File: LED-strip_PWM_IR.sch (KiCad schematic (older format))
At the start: 18 parts, among them IC1 ATTINY85-S, P1 CONN_2, P2 CONN_2, Q1 8MHz, T1 IRLR2905_DPAK, U1 TSOP38238, U2 MCP1804-SOT23-5

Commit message: Grmbl! Never trust footprints from 'some lib'...
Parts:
- IC1: footprint SO8-200 -> (none)
- Q1: footprint murata-resonators-CSTLA_T -> (none)
- R3: value 20k -> 100k
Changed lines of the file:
@@
 F 0 "Q1" H 4400 2550 50  0000 L BNN
 F 1 "8MHz" H 4550 2550 50  0000 L BNN
-F 2 "murata-resonators-CSTLA_T" H 4550 2550 50  0001 C CNN
+F 2 "" H 4550 2550 50  0001 C CNN
 F 3 "" H 4550 2400 60  0001 C CNN
 	1    4550 2400
@@
 P 4100 3750
 F 0 "R3" V 4100 3850 50  0000 C CNN
-F 1 "20k" V 4100 3700 43  0000 C CNN
+F 1 "100k" V 4100 3700 43  0000 C CNN
 F 2 "" H 4100 3750 60  0001 C CNN
 F 3 "" H 4100 3750 60  0001 C CNN
@@
 F 0 "IC1" H 1900 1800 60  0000 C CNN
 F 1 "ATTINY85-S" H 3800 1000 60  0000 C CNN
-F 2 "SO8-200" H 2050 1000 60  0000 C CNN
+F 2 "" H 2050 1000 60  0000 C CNN
 F 3 "" H 2950 1400 60  0001 C CNN
 	1    2950 1400

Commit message: Switched Schottky diode to SS14L + rounded corners.
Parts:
- DS1: value MBRS140T3G -> SS14L
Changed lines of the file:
@@
 Sheet 1 1
 Title "LED-strip_PWM_IR"
-Date "19 may 2013"
-Rev "0.4"
+Date "16 Jun 2013"
+Rev "0.43"
 Comp "2013 - blog.spitzenpfeil.org"
 Comment1 ""
@@
 P 5500 3250
 F 0 "DS1" H 5500 3350 40  0000 C CNN
-F 1 "MBRS140T3G" H 5500 3150 40  0000 C CNN
+F 1 "SS14L" H 5500 3150 40  0000 C CNN
 F 2 "~" H 5500 3250 60  0000 C CNN
 F 3 "~" H 5500 3250 60  0000 C CNN

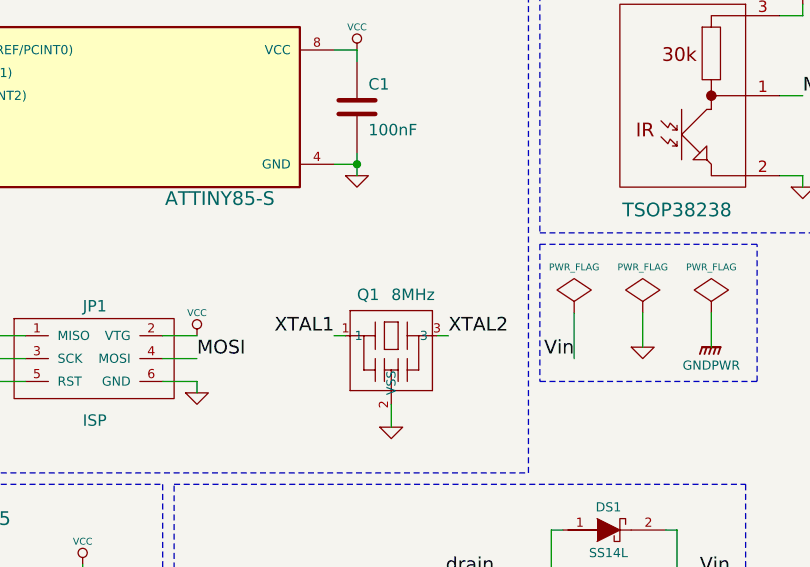
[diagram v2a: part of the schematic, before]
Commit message: Fixed resonator footprint (library part was off).
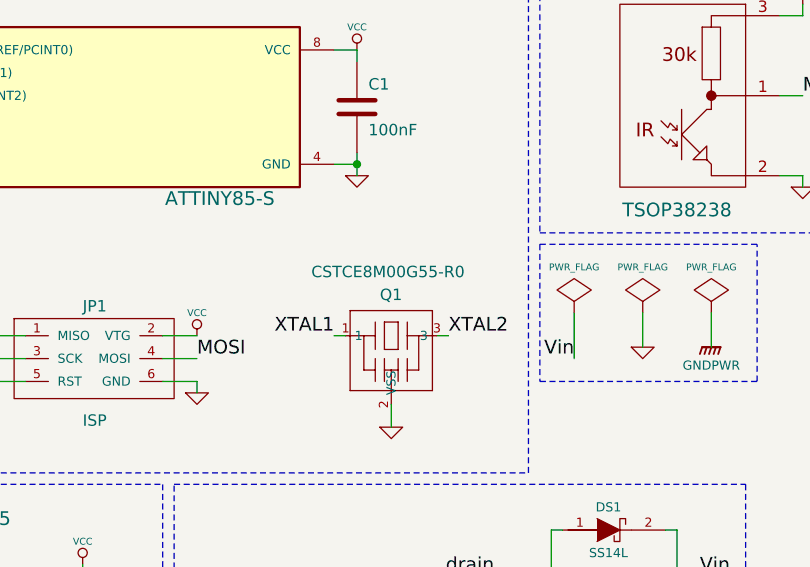
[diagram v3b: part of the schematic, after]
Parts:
- Q1: value 8MHz -> CSTCE8M00G55-R0
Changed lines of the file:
@@
 Sheet 1 1
 Title "LED-strip_PWM_IR"
-Date "16 Jun 2013"
+Date "29 Sep 2013"
 Rev "0.43"
 Comp "2013 - blog.spitzenpfeil.org"
@@
 U 1 1 4F6EC7D6
 P 4550 2400
-F 0 "Q1" H 4400 2550 50  0000 L BNN
-F 1 "8MHz" H 4550 2550 50  0000 L BNN
+F 0 "Q1" H 4500 2550 50  0000 L BNN
+F 1 "CSTCE8M00G55-R0" H 4200 2650 50  0000 L BNN
 F 2 "" H 4550 2550 50  0001 C CNN
 F 3 "" H 4550 2400 60  0001 C CNN
